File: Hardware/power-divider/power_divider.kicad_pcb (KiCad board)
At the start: 4 copper layers, 40 x 51.9 mm, 22 parts, among them J1 Conn_Coaxial, J2 Conn_Coaxial, J3 Conn_Coaxial

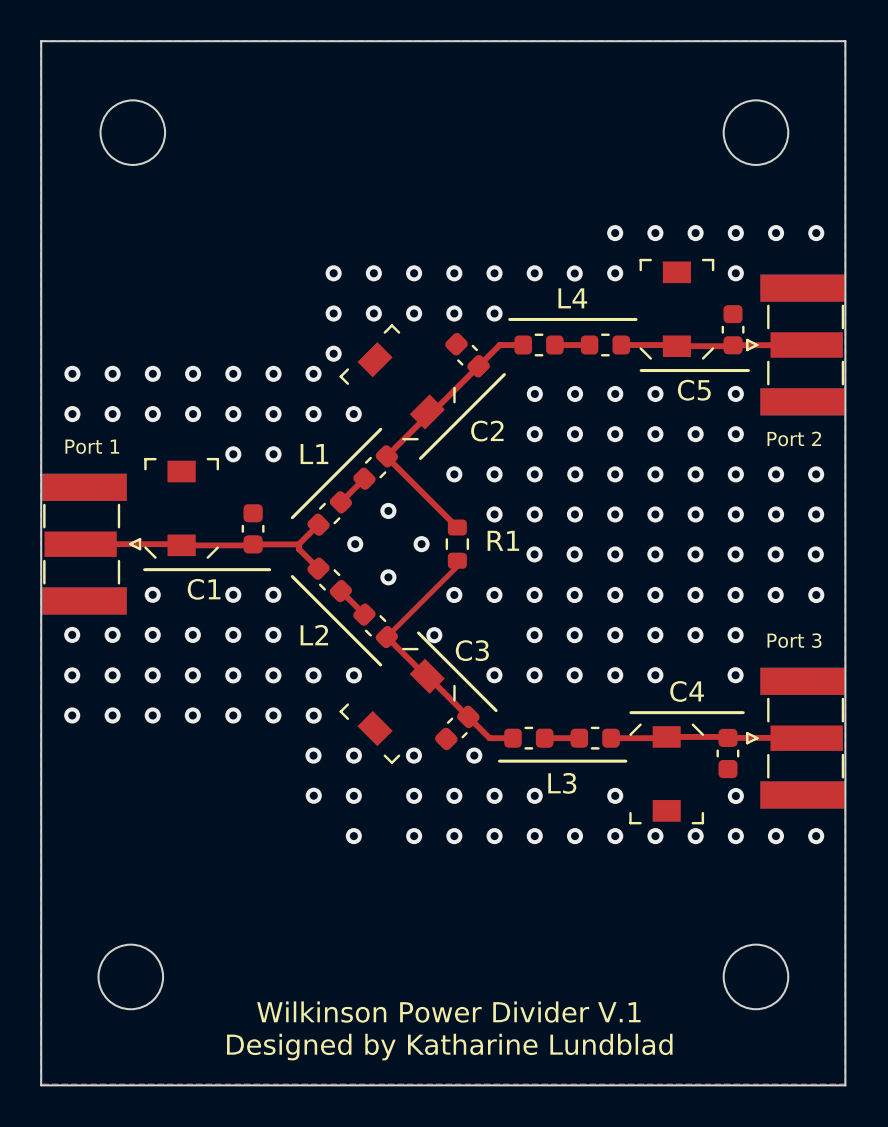
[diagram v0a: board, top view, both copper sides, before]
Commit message: PD: Silkscreen Color Tweak
- Changed bottom silkscreen to green
- Aligned board edges and fill polygon to grid
- Rounded the corners
- Added box for label
- Moved R1 slightly closer
- Increased default netclass clearance from 0.2 to 0.6mm
- Set polygon clearance to 0 to fill to edge of holes
- Added SMA connector models
- Fixed Schematic-PCB parity
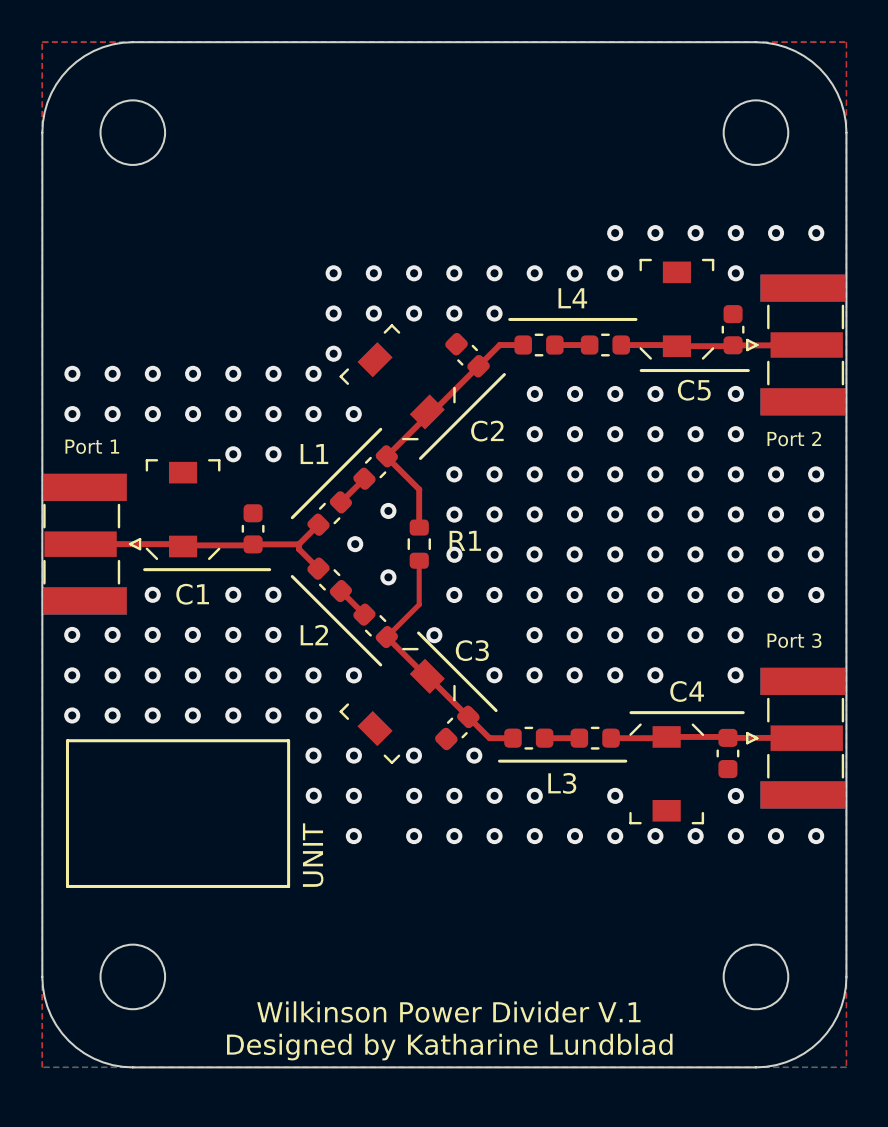
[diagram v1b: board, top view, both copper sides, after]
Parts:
- removed the C1 at (122.4, 75.7)
- added C4: C_Trim, Capacitor_SMD:C_Trimmer_Sprague-Goodman_SGC3, F.Cu at (122.5, 75.8)
- J1, J2, J3: footprint Connector_Coaxial:SMA_Samtec_SMA-J-P-X-ST-EM1_EdgeMount -> OTS_Tag:SMA_Samtec_SMA-J-P-X-ST-EM1_EdgeMount
- moved R1 1.89 mm to (134.2, 77.5)
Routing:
- net Net-(C5-Pad1): track 14.2 -> 13.4 mm
- net Net-(C6-Pad1): track 13.6 -> 12.8 mm
- net GND: vias 151 -> 153
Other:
- board size 40 x 51.9 mm -> 40 x 51 mm
- board text added: "C1"
- board text added: "UNIT"
